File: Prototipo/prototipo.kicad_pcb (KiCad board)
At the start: 2 copper layers, 148 parts, among them Q11_1 MMBT2222A, Q11_2 MMBT2907A, Q11_3 MMBT2222A, Q12_1 MMBT2222A, Q12_2 MMBT2907A, Q12_3 MMBT2222A, Q1_1 MMBT2222A, Q1_2 MMBFJ201, Q21_1 MMBT2222A, Q21_2 MMBT2907A, Q21_3 MMBT2222A, Q22_1 MMBT2222A, Q22_2 MMBT2907A, Q22_3 MMBT2222A, Q2_1 MMBT2222A, Q2_2 MMBFJ201, Q31_1 MMBT2222A, Q31_2 MMBT2907A, Q31_3 MMBT2222A, Q32_1 MMBT2222A, Q32_2 MMBT2907A, Q32_3 MMBT2222A, Q3_1 MMBT2222A, Q3_2 MMBFJ201

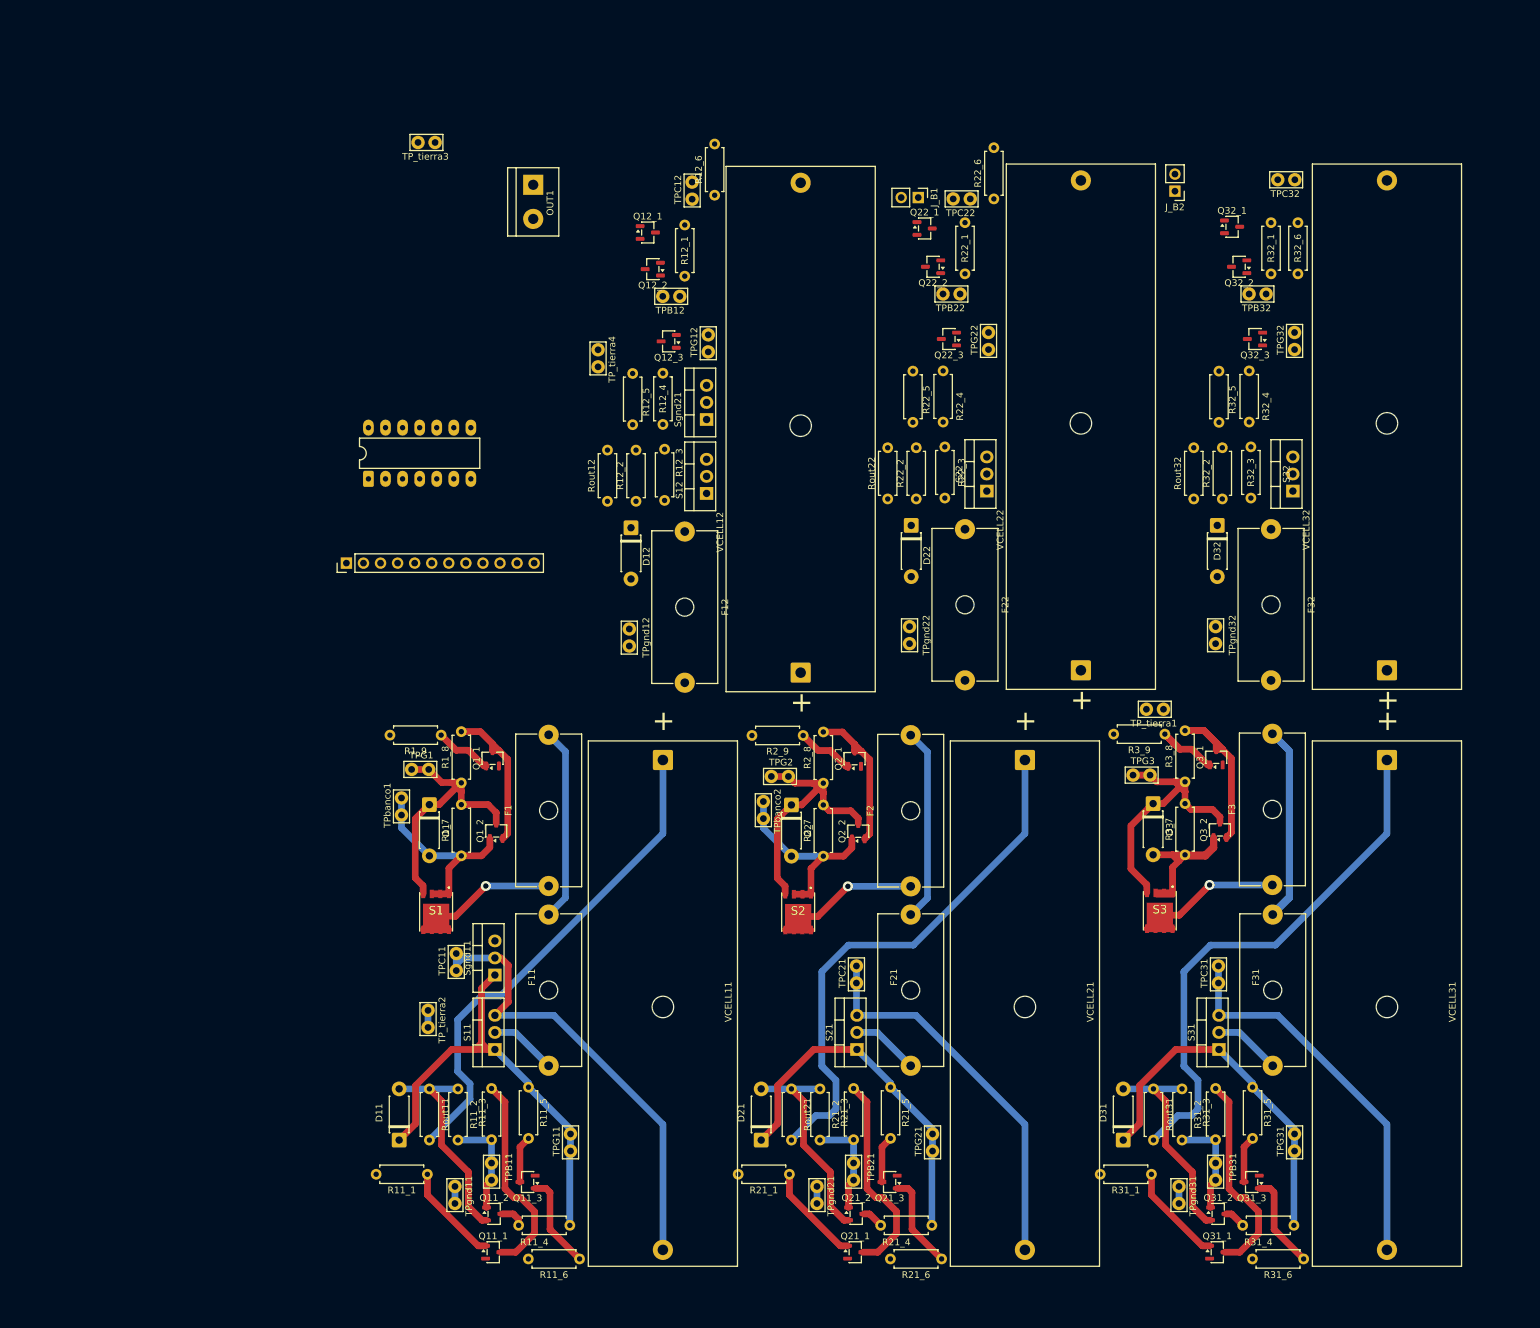
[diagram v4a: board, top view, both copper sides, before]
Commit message: primer propuesta de conexion de entradas
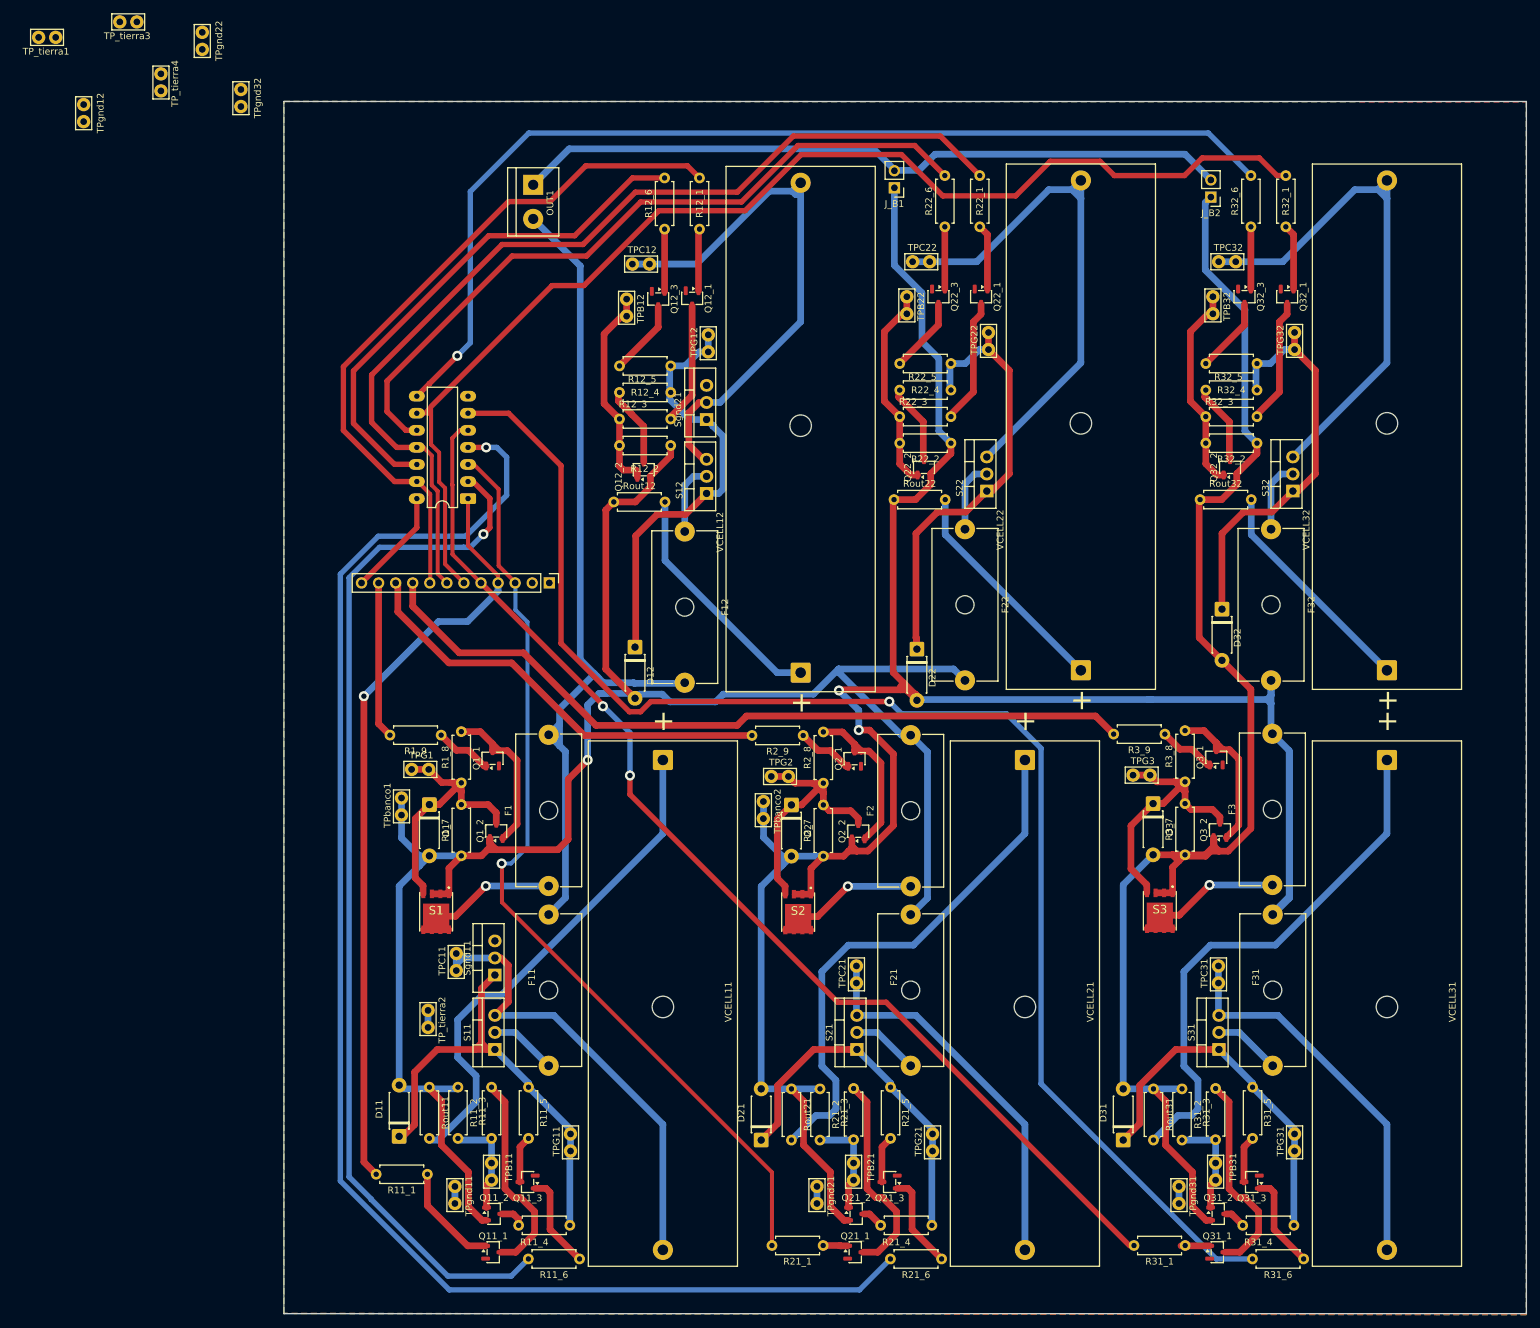
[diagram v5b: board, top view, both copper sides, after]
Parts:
- moved TP_tierra1 192.8 mm to (309.1, 129.2)
- moved TPgnd32 165.6 mm to (339.2, 139.5)
- moved TPgnd22 137.5 mm to (333.5, 131.0)
- moved TPgnd12 112.6 mm to (315.9, 141.8)
- moved TP_tierra4 76.9 mm to (327.4, 137.2)
- moved TP_tierra3 47.9 mm to (321.2, 126.9)
- moved IN1 30.3 mm to (385.1, 210.4), turned to -90 degrees
- moved Q22_2 29.9 mm to (440.9, 193.2), turned to 90 degrees
- moved Q32_2 29.9 mm to (486.4, 193.2), turned to 90 degrees
- moved Q12_2 29.9 mm to (399.2, 193.6), turned to 90 degrees
- moved D22 18.4 mm to (439.9, 220.2)
- moved D12 17.8 mm to (397.9, 219.9)
- moved A1 15.1 mm to (373.1, 197.8), turned to 180 degrees
- moved TPC12 13.8 mm to (400.1, 162.9), turned to 180 degrees
- moved TPC32 13.7 mm to (487.3, 162.6), turned to 180 degrees
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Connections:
- IN1 pad 11: Vc3 -> Vc1
- IN1 pad 12: 0 -> VCC
- IN1 pad 2: VCC -> unconnected-(IN1-Pin_2-Pad2)
- IN1 pad 3: Vc_11 -> Vc_21
- IN1 pad 4: Vc_21 -> Vc_11
- IN1 pad 9: Vc1 -> Vc3
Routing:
- net /celda_21/bus_pos: track 119.4 -> 353.0 mm, vias 0 -> 2
- net /celda_21/Vcontrol_neg: track 0.00 -> 222.4 mm, vias 0 -> 1
- net /celda_31/Vcontrol_neg: track 0.00 -> 214.8 mm, vias 0 -> 1
- net /celda_11/bus_pos: track 91.0 -> 286.7 mm, vias 0 -> 1
- net Vc_32: track 0.00 -> 183.6 mm
- net Vc_31: track 0.00 -> 169.1 mm, vias 0 -> 2
- net /celda_32/Vcontrol_neg: track 0.00 -> 156.1 mm, vias 0 -> 1
- net /celda_11/Vcontrol_neg: track 0.00 -> 155.7 mm, vias 0 -> 1
- net /celda_31/bus_pos: track 61.6 -> 210.5 mm
- net Vc_22: track 0.00 -> 145.6 mm
- net Vc_21: track 0.00 -> 139.5 mm, vias 0 -> 1
- net Vc3: track 0.00 -> 116.8 mm
- net Vc_11: track 0.00 -> 114.0 mm, vias 0 -> 1
- net /celda_22/Vcontrol_neg: track 0.00 -> 109.5 mm
- net Net-(J_B1-Pin_2): track 0.00 -> 107.1 mm
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- added copper zone on B.Cu, net 0
- added copper zone on F.Cu, net 0
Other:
- board outline added: 184.9 x 180.4 mm

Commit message: sube archivos de drill
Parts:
- moved TP_tierra1 47.2 mm to (351.9, 149.3)
- moved TPgnd22 40.1 mm to (370.6, 146.2)
- moved TP_tierra3 40.1 mm to (358.3, 142.2)
- moved TP_tierra4 40.1 mm to (364.4, 152.4)
- moved TPgnd12 40.1 mm to (352.9, 157.0)
- moved TPgnd32 30.4 mm to (360.4, 161.3)
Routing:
- removed copper zone on B.Cu, net 0

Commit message: acomodo la bornera
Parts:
- moved Q31_2 120.3 mm to (515.1, 187.9)
- moved D32 120.3 mm to (515.7, 98.0)
- moved Q12_1 120.3 mm to (436.9, 51.7)
- moved Q22_1 120.3 mm to (479.9, 51.5)
- moved Q32_1 120.3 mm to (525.4, 51.5)
- moved R12_4 120.3 mm to (426.0, 65.7)
- moved R22_1 120.3 mm to (479.7, 41.0)
- moved R32_1 120.3 mm to (525.2, 41.0)
- moved TPbanco1 120.3 mm to (393.6, 126.0)
- moved D12 120.3 mm to (428.4, 103.6)
- moved F2 120.3 mm to (469.4, 139.2)
- moved F3 120.3 mm to (523.2, 139.0)
- moved Q11_2 120.3 mm to (407.4, 187.9)
- moved Q11_3 120.3 mm to (412.4, 183.2)
- moved Q1_2 120.3 mm to (407.7, 130.9)
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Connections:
- IN1 pad 10: Vc2 -> Vc1
- IN1 pad 11: Vc1 -> VCC
- IN1 pad 12: VCC -> 0
- IN1 pad 2: unconnected-(IN1-Pin_2-Pad2) -> Vc_21
- IN1 pad 3: Vc_21 -> Vc_11
- IN1 pad 4: Vc_11 -> Vc_31
- IN1 pad 5: Vc_31 -> Vc_32
- IN1 pad 6: Vc_32 -> Vc_22
- IN1 pad 7: Vc_22 -> Vc_12
- IN1 pad 8: Vc_12 -> Vc3
- IN1 pad 9: Vc3 -> Vc2
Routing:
- net Vc_11: track 114.0 -> 119.1 mm
- net /celda_11/bus_neg: track 129.7 -> 132.1 mm
- net Vc_12: track 105.7 -> 107.2 mm
- net /celda_31/Vcontrol_neg: track 214.8 -> 215.9 mm
- net Vc_32: track 183.6 -> 184.6 mm
- net Vc_22: track 145.6 -> 146.6 mm
- net VCC: track 16.0 -> 14.9 mm
- net Vc3: track 116.8 -> 115.8 mm
- net Vc2: track 64.8 -> 63.7 mm
- net /celda_11/bus_pos: track 286.7 -> 285.8 mm
- net Vc_21: track 139.5 -> 140.1 mm
- net /celda_21/bus_pos: track 353.0 -> 352.4 mm

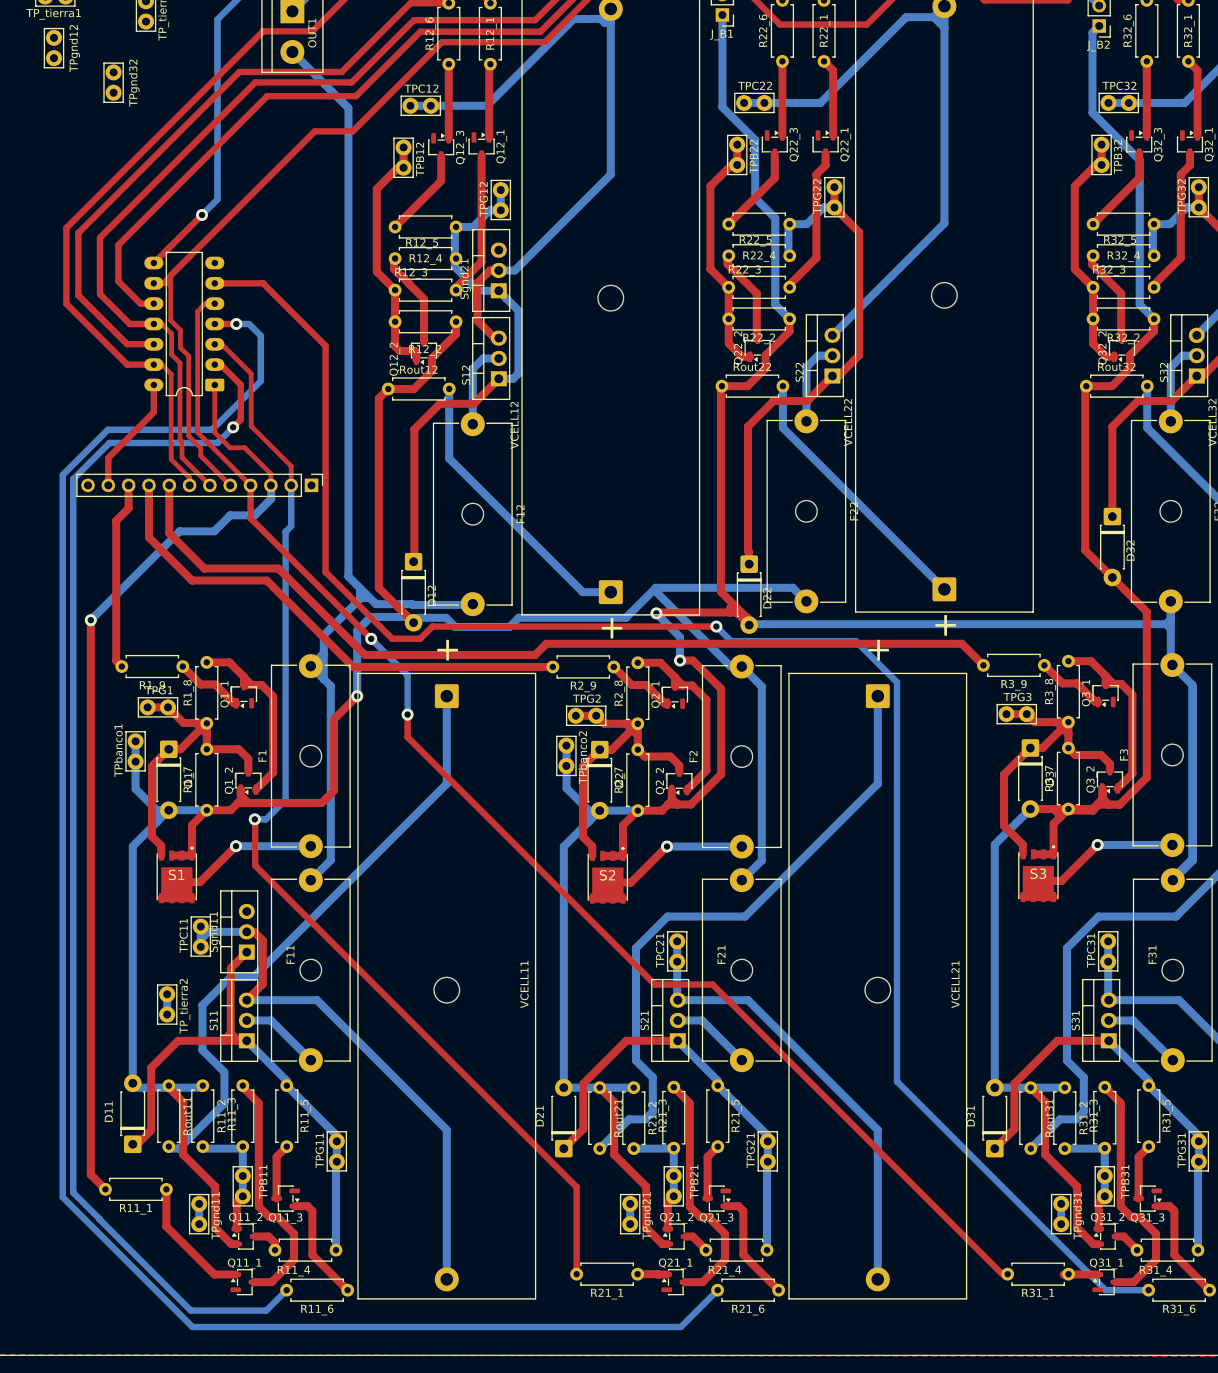
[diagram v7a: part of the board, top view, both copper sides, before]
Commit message: pongo la bonera toda en una sola capa
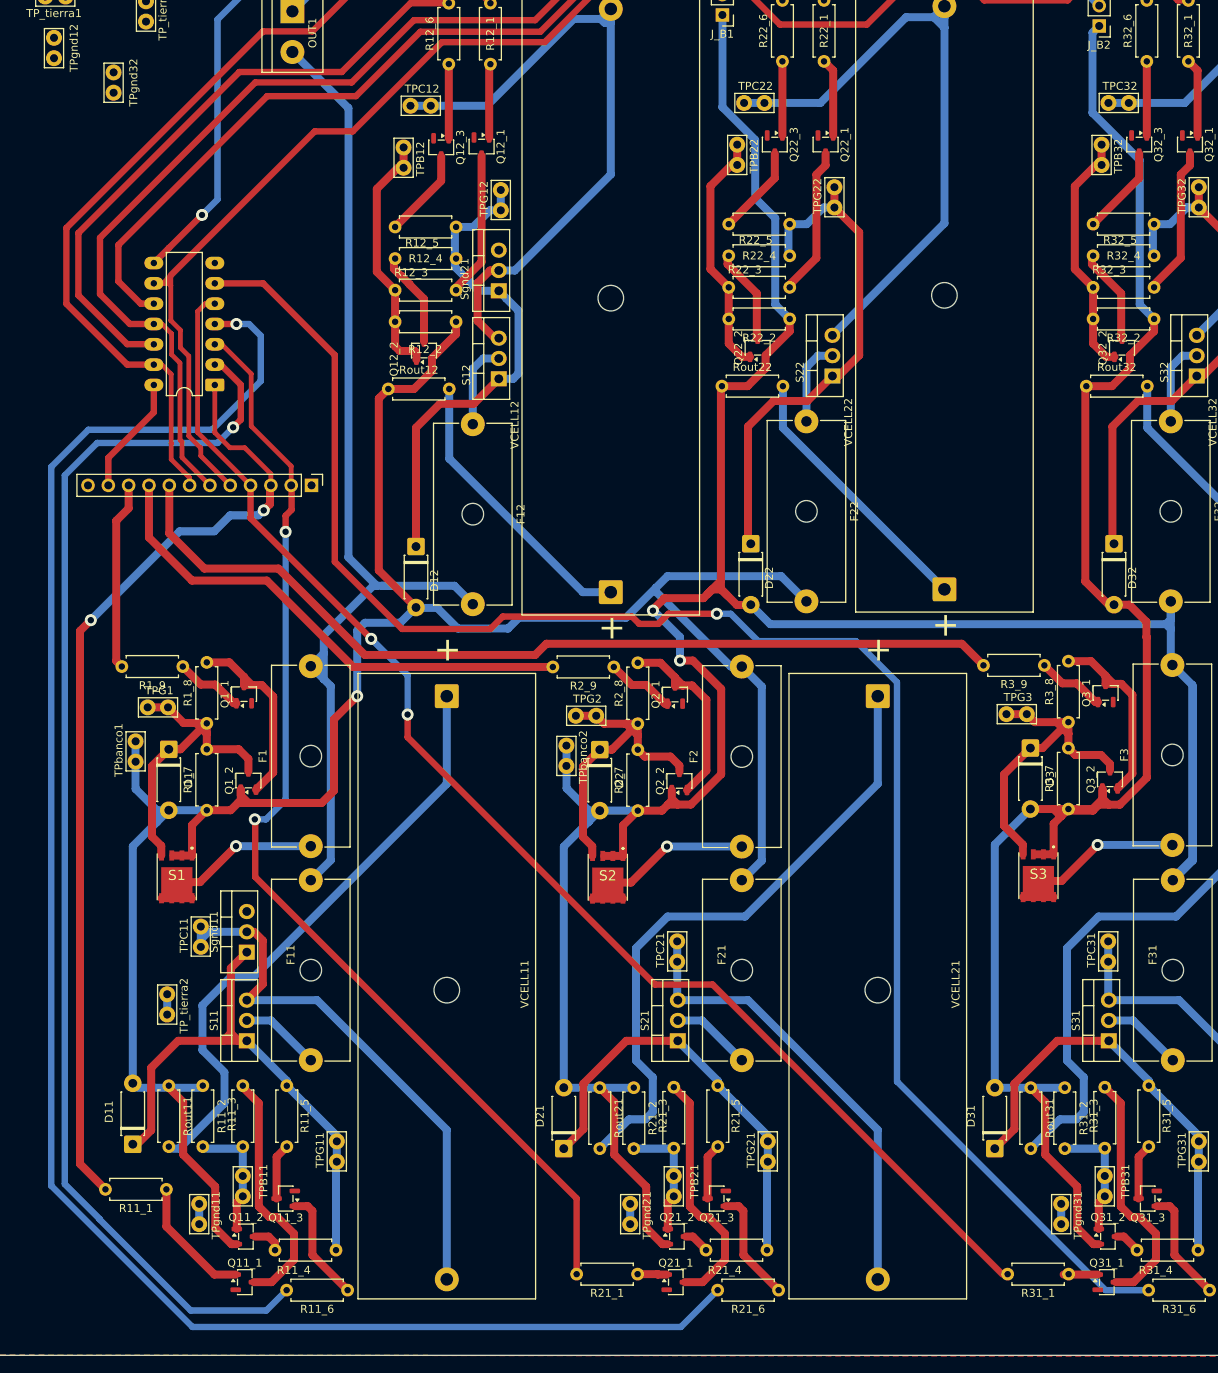
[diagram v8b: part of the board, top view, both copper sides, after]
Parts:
- moved D32 3.41 mm to (515.9, 101.3)
- moved D22 2.56 mm to (470.5, 101.3)
- moved D12 1.92 mm to (428.6, 101.7)
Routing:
- net /celda_32/gate: track 61.9 -> 65.4 mm
- net /celda_21/Vcontrol_neg: track 222.4 -> 225.0 mm
- net /celda_22/gate: track 67.9 -> 65.5 mm
- net /celda_12/gate: track 65.0 -> 62.9 mm
- net /celda_11/Vcontrol_neg: track 155.7 -> 157.5 mm
- net /celda_31/bus_pos: track 210.5 -> 212.1 mm
- net Vc_11: track 119.1 -> 120.5 mm, vias 1 -> 2
- net /celda_11/bus_neg: track 132.1 -> 131.5 mm
- net Vc_21: vias 1 -> 2
